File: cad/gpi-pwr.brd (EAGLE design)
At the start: 133 x 73.5 mm, 87 parts, among them CN1 HEADER-1X2, CN2 HEADER-3X1, CN3 HEADER-1X2.4, Q1 MOSFETTO247REV, Q3 MOSFETTO247REV, Q5 MOSFETTO247REV, Q6 MOSFETTO247REV, Q7 MOSFETTO247REV, Q8 MOSFETTO247REV, U1 ACS709, U2 ACS709, U3 ACPL-P346P346, U4 ACPL-P346P346, U5 ACPL-P346P346, U6 ACPL-P346P346, U7 ACPL-P346P346, U8 ACPL-P346P346

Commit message: tweak
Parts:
- added C26: .1u, jaw:SMD2220
- added R25: 1M, jaw:SMD1206
- C3: value .1u CER -> .1u
- moved C23 9.20 mm to (43.0, 7.00), flipped to the bottom
- moved C24 3.35 mm to (38.1, 10.5), flipped to the bottom, turned to 180 degrees
- moved C3 0.50 mm to (85.1, 71.6)
- flipped C21 to the bottom
- flipped C22 to the bottom
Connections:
- net GND: now also C26.P$2, R25.1
- net N$7: now also R25.2
- net V1KDC: now also C26.P$1
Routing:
- net GND: track 358.0 -> 390.6 mm, vias 24 -> 48
- net V1KDC: track 138.9 -> 146.5 mm
- net VCC: track 177.3 -> 184.8 mm
- net N$7: track 43.5 -> 49.0 mm
- net VCCM: track 132.1 -> 128.2 mm
- net ADC3: track 78.0 -> 80.8 mm
- net ADC5: track 13.9 -> 15.3 mm

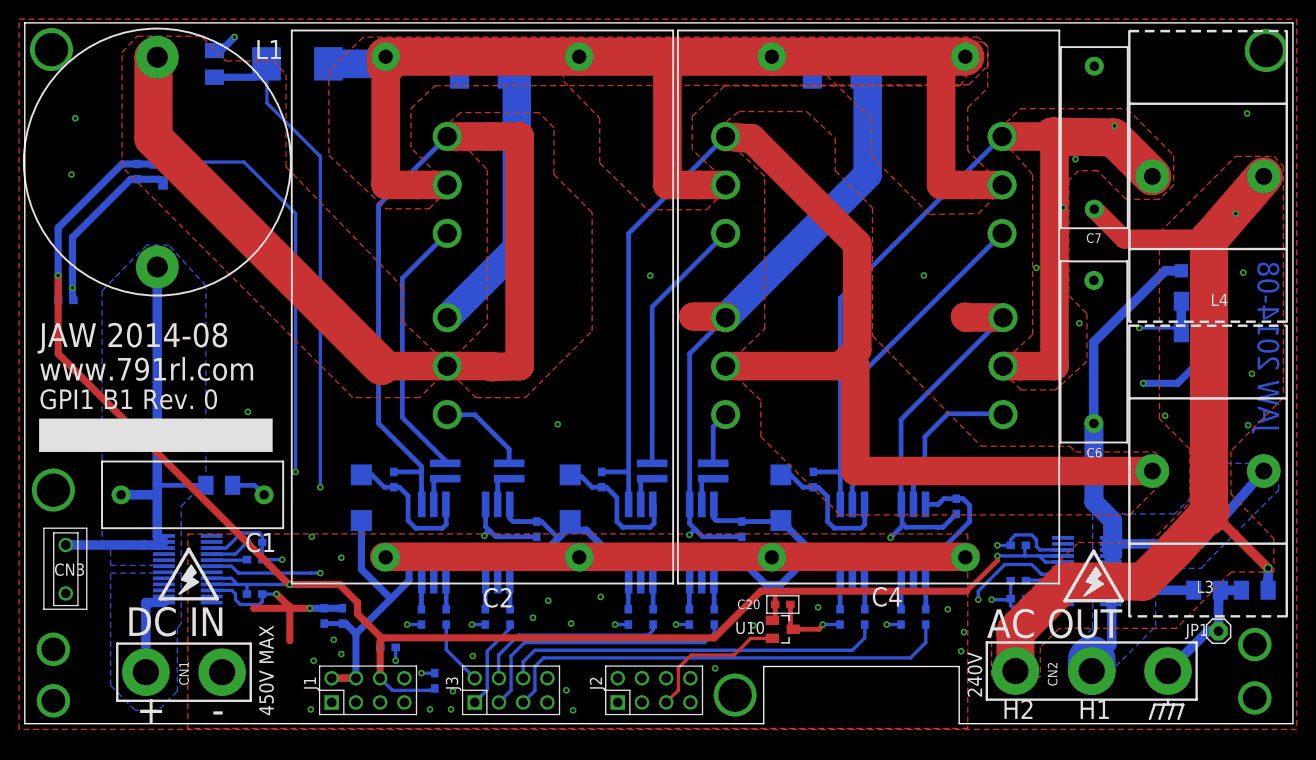
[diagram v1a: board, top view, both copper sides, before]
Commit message: better output filter
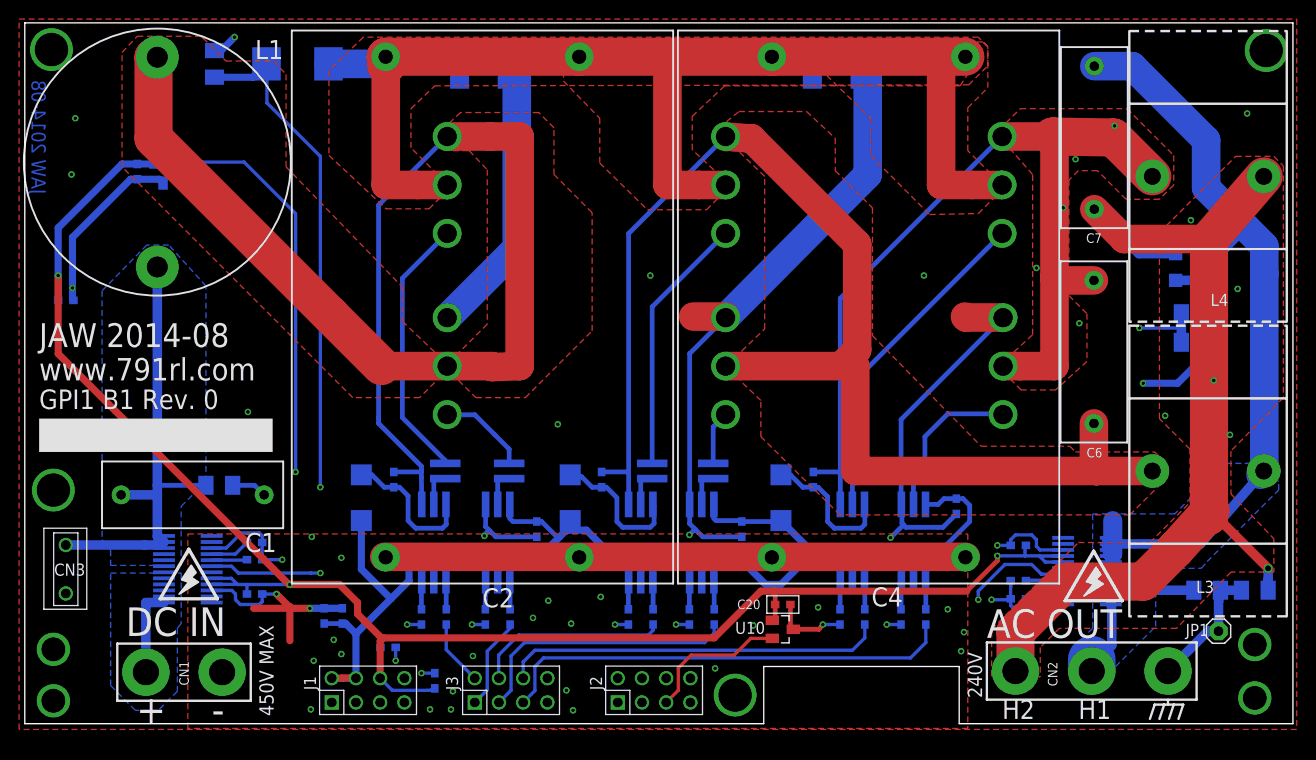
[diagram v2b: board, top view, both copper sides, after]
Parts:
- moved D2 3.20 mm to (120.7, 50.4), turned to 90 degrees
- moved D1 1.46 mm to (124.1, 50.4), turned to 90 degrees
- moved R12 1.30 mm to (122.7, 45.5)
- moved R10 1.00 mm to (122.7, 42.5)
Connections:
- net GND: no longer C6.P$2, C7.P$1
- net N$15: now also C6.P$1
- net N$16: now also C6.P$2
- net N$24: now also C7.P$1; no longer C6.P$1
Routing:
- net N$24: track 55.9 -> 82.3 mm
- net N$15: track 133.2 -> 138.7 mm
- net N$16: track 99.2 -> 103.4 mm
- net GND: track 390.6 -> 389.6 mm
- net N$9: track 6.10 -> 6.90 mm

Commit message: tweak sent to fab
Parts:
- C1, C6, C7: value .33u -> .47u
- C13, C14: value (none) -> 1u
- R1: value 1M 2kV -> 2M 2kV
- R10: value 3k -> 3k3; device jaw:SMD1206 -> jaw:SMD0603
- R23, R24: value (none) -> 4r7
- R3, R4: value 330k -> 392k
- R5: value 3k -> 3k3
- moved R10 0.72 mm to (122.1, 42.1)
- moved D2 0.20 mm to (120.5, 50.4)
- moved D1 0.10 mm to (124.2, 50.4)
- moved R12 0.10 mm to (122.8, 45.5)
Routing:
- net GND: track 389.6 -> 388.7 mm
- net N$25: track 103.0 -> 102.8 mm, vias 6 -> 8
- net N$16: vias 5 -> 11
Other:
- outline, holes or cut-outs redrawn

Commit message: viper package
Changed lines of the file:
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@@
 <layer number="19" name="Unrouted" color="6" fill="1" visible="yes" active="yes"/>
 <layer number="20" name="Dimension" color="15" fill="1" visible="yes" active="yes"/>
-<layer number="21" name="tPlace" color="7" fill="1" visible="no" active="yes"/>
-<layer number="22" name="bPlace" color="7" fill="1" visible="yes" active="yes"/>
+<layer number="21" name="tPlace" color="7" fill="1" visible="yes" active="yes"/>
+<layer number="22" name="bPlace" color="7" fill="1" visible="no" active="yes"/>
 <layer number="23" name="tOrigins" color="15" fill="1" visible="yes" active="yes"/>
 <layer number="24" name="bOrigins" color="15" fill="1" visible="yes" active="yes"/>
@@
 <rectangle x1="1.5" y1="31" x2="26" y2="34.5" layer="21"/>
 <wire x1="119.9" y1="4.5" x2="119.9" y2="5" width="0.25" layer="21"/>
-<wire x1="2" y1="23" x2="6.5" y2="23" width="0.1" layer="21"/>
-<wire x1="6.5" y1="23" x2="6.5" y2="14.5" width="0.1" layer="21"/>
-<wire x1="6.5" y1="14.5" x2="2" y2="14.5" width="0.1" layer="21"/>
-<wire x1="2" y1="14.5" x2="2" y2="23" width="0.1" layer="21"/>
+<wire x1="2" y1="23" x2="6.5" y2="23" width="0.1" layer="21" style="shortdash"/>
+<wire x1="6.5" y1="23" x2="6.5" y2="14.5" width="0.1" layer="21" style="shortdash"/>
+<wire x1="6.5" y1="14.5" x2="2" y2="14.5" width="0.1" layer="21" style="shortdash"/>
+<wire x1="2" y1="14.5" x2="2" y2="23" width="0.1" layer="21" style="shortdash"/>
 <text x="2.2" y="70" size="1.5" layer="16" ratio="15" rot="MR270">JAW 2014-08</text>
 <text x="2.2" y="70" size="1.5" layer="30" ratio="15" rot="MR270">JAW 2014-08</text>
+<wire x1="8" y1="21.5" x2="27.2" y2="21.5" width="0.1" layer="21" style="shortdash"/>
+<wire x1="8" y1="31.5" x2="27.2" y2="31.5" width="0.1" layer="21" style="shortdash"/>
+<wire x1="8" y1="21.6" x2="8" y2="31.5" width="0.1" layer="21" style="shortdash"/>
+<wire x1="27.2" y1="31.5" x2="27.2" y2="21.5" width="0.1" layer="21" style="shortdash"/>
 </plain>
 <attributes>

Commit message: tweak text
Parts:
- C19, C20: value (none) -> .1u
- C21: value 1u -> 1u 25V
- C22: value 10u -> 10u 25V
- R5: device jaw:SMD1206 -> jaw:SMD0603
- moved R5 0.81 mm to (20.6, 71.3)
- moved L3 0.50 mm to (123.6, 29.0)
- moved L4 0.50 mm to (123.6, 59.9)
- moved C7 0.47 mm to (111.7, 64.0)
- moved C6 0.43 mm to (111.7, 41.5)
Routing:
- net ADC2: track 93.6 -> 91.4 mm
- net N$16: track 103.4 -> 102.0 mm
- net N$25: track 102.8 -> 104.0 mm
- net N$24: track 82.2 -> 83.1 mm
- net N$15: track 138.7 -> 137.8 mm

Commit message: gate snubbers
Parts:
- added D10, D11, D6, D7, D8, D9: DIODESOD-323, jaw:SOD-323
- R19, R20, R21, R22, R23, R24: device jaw:SMD0612 -> jaw:SMD0508
- moved R19 1.12 mm to (64.8, 29.5)
- moved R20 1.12 mm to (87.0, 29.5)
- moved R21 1.12 mm to (93.4, 29.5)
- moved R22 1.12 mm to (71.2, 29.5)
- moved R23 1.12 mm to (49.8, 29.5)
- moved R24 1.03 mm to (43.2, 29.5)
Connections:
- net N$19: now also D9.A
- net N$2: now also D9.C
- net N$20: now also D8.A
- net N$21: now also D10.A
- net N$22: now also D11.A
- net N$24: now also D1.C; no longer D1.A
- net N$25: now also D2.C; no longer D2.A
- net N$43: now also D11.C
- net N$44: now also D8.C
- net N$46: now also D10.C
- net N$47: now also D7.C
- net N$48: now also D7.A
- net N$5: now also D6.A
- net N$6: now also D6.C
- net N$9: now also D1.A, D2.A; no longer D1.C, D2.C
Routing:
- net GND: track 388.8 -> 343.4 mm
- net N$2: track 3.84 -> 6.61 mm
- net N$43: track 3.84 -> 6.51 mm
- net N$46: track 3.84 -> 6.51 mm
- net N$44: track 3.84 -> 6.51 mm
- net N$6: track 3.87 -> 6.51 mm
- net N$47: track 3.92 -> 6.47 mm
- net N$19: track 27.3 -> 29.5 mm
- net N$21: track 12.1 -> 14.2 mm
- net N$20: track 5.66 -> 7.77 mm
- net N$22: track 30.1 -> 32.2 mm
- net N$4: track 135.4 -> 133.6 mm
- net N$5: track 9.50 -> 11.2 mm
- net N$48: track 27.9 -> 29.6 mm

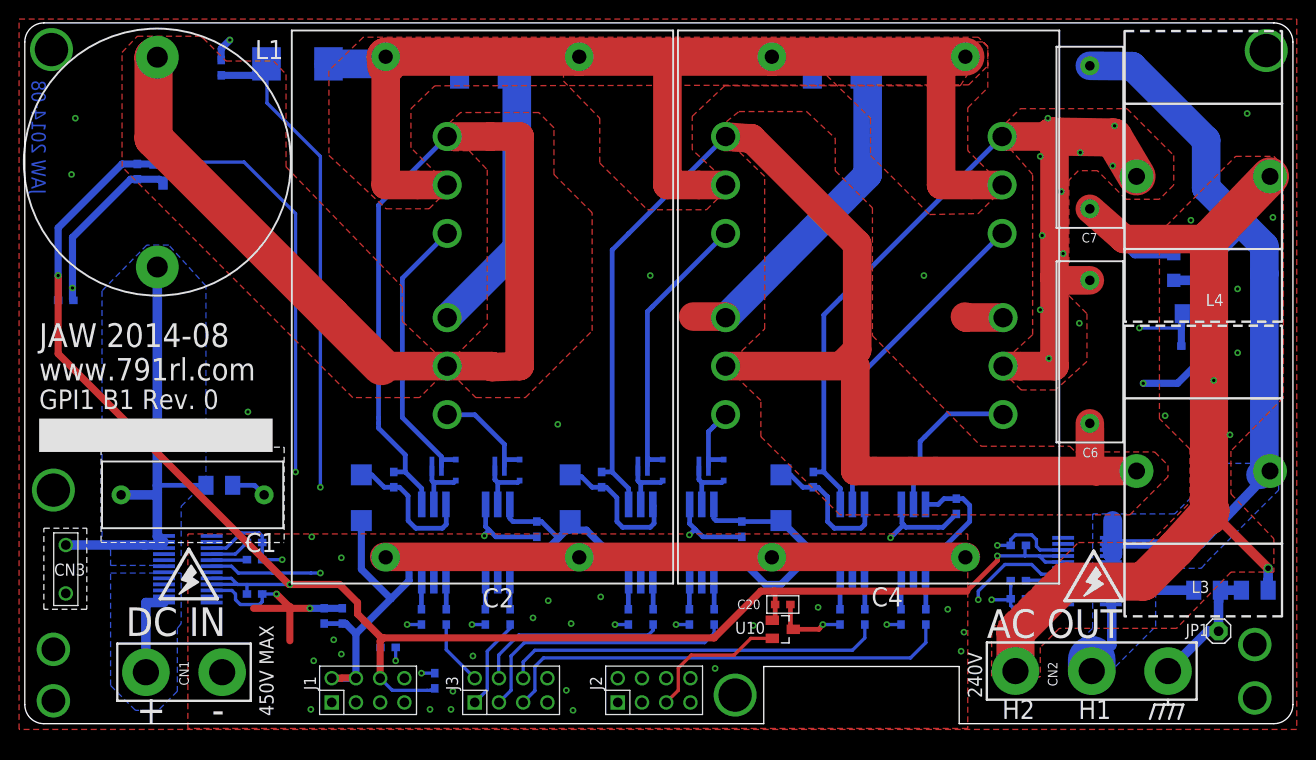
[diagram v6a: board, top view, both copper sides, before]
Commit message: op-amps on v-divs
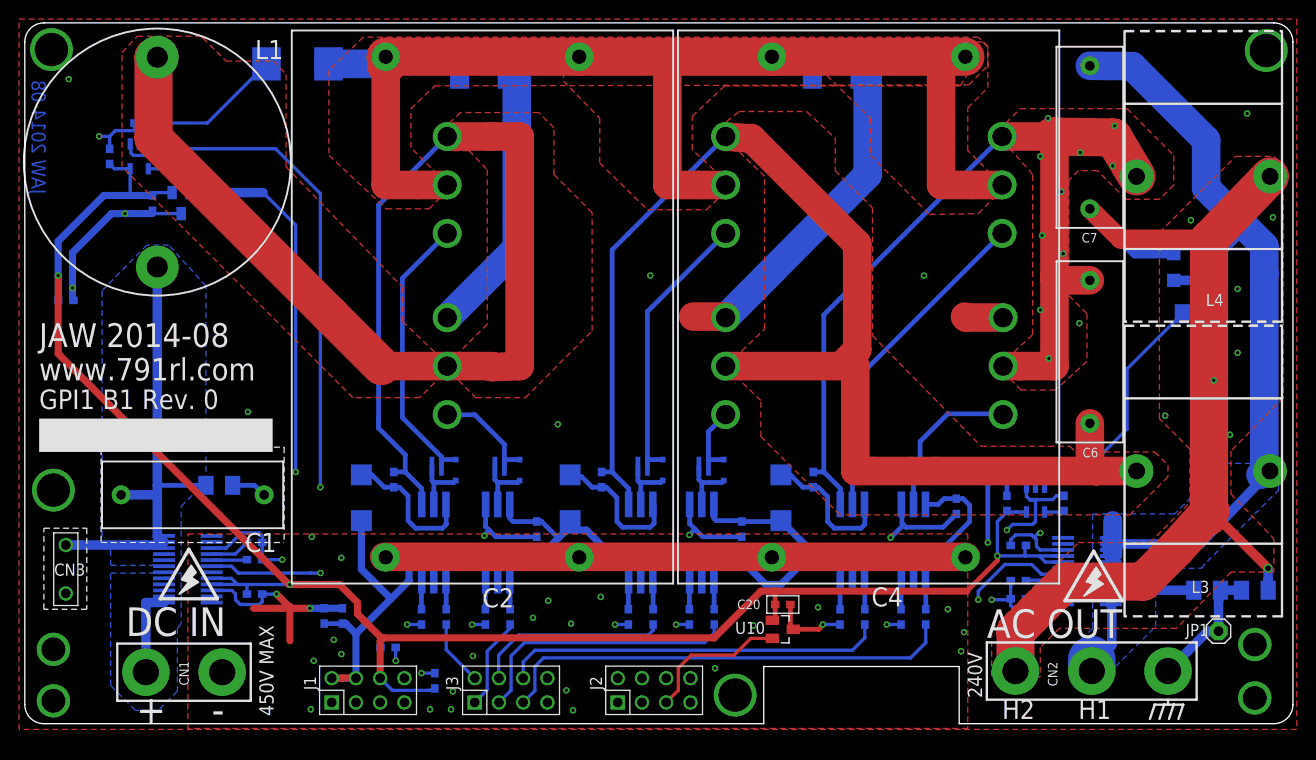
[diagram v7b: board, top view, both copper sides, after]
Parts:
- added C27, C28: .1u, jaw:SMD0603
- added R26, R27: 22, jaw:SMD0603
- added U11, U12: MAX4452, jaw:SOT-23-5
- R12: value 600k -> 592k
- U10, U9: value (none) -> LM61
- moved R10 20.1 mm to (106.5, 29.5), turned to 0 degrees
- moved R5 10.1 mm to (12.3, 65.5), turned to 180 degrees
- moved U9 3.72 mm to (16.4, 57.1)
- moved C19 3.67 mm to (13.4, 57.1)
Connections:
- new net N$51: R26.1, U12.4
- new net N$52: R27.1, U11.4
- new net OP1: R1.P$1, R5.2, U11.3
- new net OP2: R10.1, R12.2, U12.3
- net ADC2: now also R27.2, U11.1; no longer R1.P$1, R5.2
- net ADC3: now also R26.2, U12.1; no longer R10.1, R12.2
- net GND: now also C27.2, C28.2, U11.2, U12.2
- net VCC: now also C27.1, C28.1, U11.5, U12.5
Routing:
- net OP2: track 0.00 -> 26.8 mm
- net ADC3: track 80.9 -> 60.5 mm
- net OP1: track 0.00 -> 17.1 mm
- net VCC: track 184.8 -> 197.0 mm
- net GND: track 343.4 -> 353.8 mm
- net ADC4: track 87.6 -> 83.6 mm
- net N$52: track 0.00 -> 2.26 mm
- net N$51: track 0.00 -> 2.07 mm
- net ADC2: track 91.4 -> 93.4 mm

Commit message: zoned grounds
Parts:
- added Z1: SHORT, jaw:SHORT
- moved C27 0.20 mm to (9.10, 62.0)
- moved U10 0.10 mm to (79.5, 12.5)
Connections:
- new net GNDA: C10.1, C11.1, C12.2, C19.2, C20.2, C23.2, C24.2, C25.2, C27.2, C28.2, C5.1, C8.1, C9.2, R10.2, R5.1, U1.15, U1.22, U10.3, U11.2, U12.2, U2.15, U2.22, U9.3, Z1.P$1
- new net GNDM: C13.2, C15.2, C17.2, C21.2, C22.2, J1.1, J1.3, J1.5, R13.2, R15.2, R17.2, R2.2, R7.2, R9.2, U3.VE, U5.VE, U7.VE, Z1.P$2
- net GND: no longer C10.1, C11.1, C12.2, C13.2, C15.2, C17.2, C19.2, C20.2, C21.2, C22.2, C23.2, C24.2, C25.2, C27.2, C28.2, C5.1, C8.1, C9.2, J1.1, J1.3, J1.5, R10.2, R13.2, R15.2, R17.2, R2.2, R5.1, R7.2, R9.2, U1.15, U1.22, U10.3, U11.2, U12.2, U2.15, U2.22, U3.VE, U5.VE, U7.VE, U9.3
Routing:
- net GND: track 353.8 -> 100.6 mm, vias 48 -> 8
- net GNDA: track 0.00 -> 115.1 mm, vias 0 -> 20
- net GNDM: track 0.00 -> 46.0 mm, vias 0 -> 44
- net VCC: track 197.0 -> 195.6 mm
- net ADC6: track 48.0 -> 47.5 mm
- added copper zone on layer 15, net GNDA
- added copper zone on layer 2, net GNDA
- added copper zone on layer 1, net GNDM
- added copper zone on layer 2, net GNDM
- removed copper zone on layer 1, net GND
- removed copper zone on layer 15, net GND
